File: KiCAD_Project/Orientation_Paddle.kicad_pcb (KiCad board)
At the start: 2 copper layers, 158.7 x 47 mm, 72 parts, among them J1 1-0001205, J2 1-0001156, J3 1-0001156, J4 NP_Conn_01x02_Relief, J5 NP_Conn_01x02_Relief, J6 NP_Conn_01x04, J7 NP_Conn_01x02, J8 1-0000050, J9 1-0000190, Q1 1-0001670, U1 1-0001471, U2 1-0000207, U3 1-0000785, U4 1-0000446, Y1 1-0000721

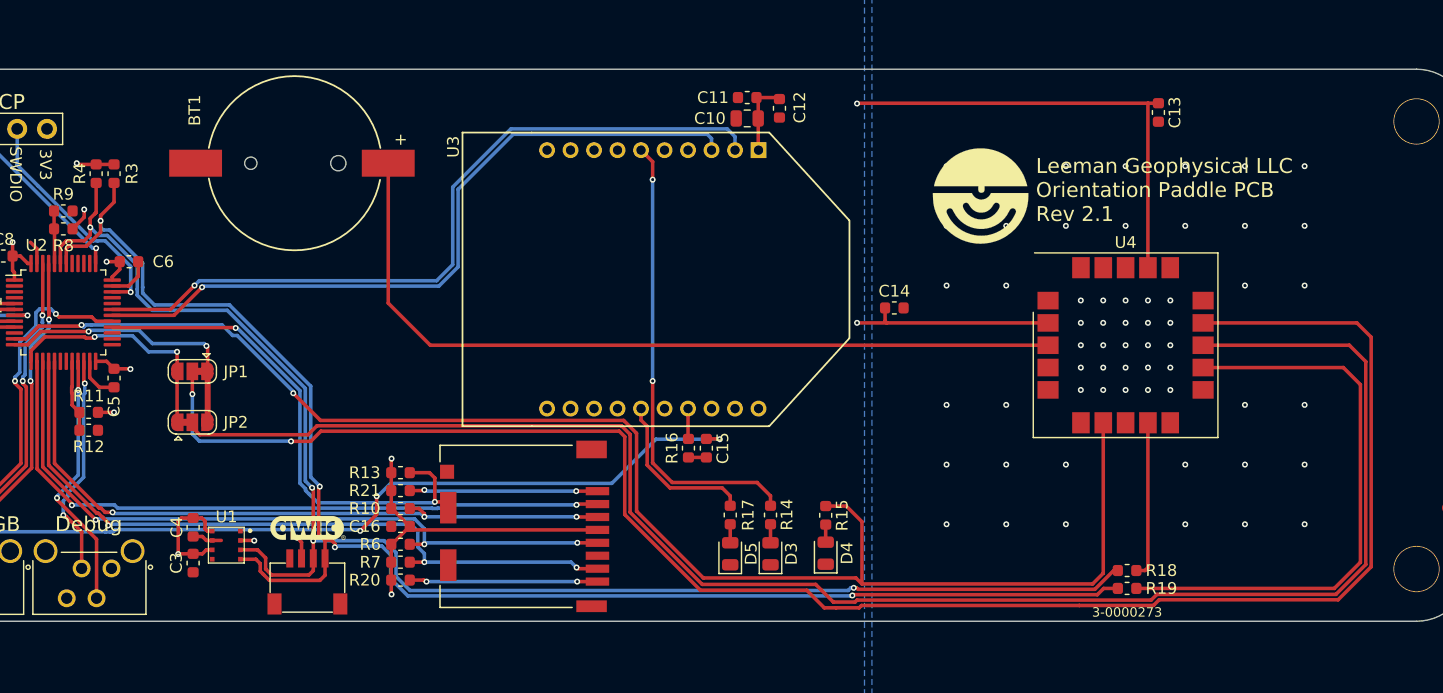
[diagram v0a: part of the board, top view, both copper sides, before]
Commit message: Rev 2.2 Changes: - Issue #2 (Swapped to Push Push SD Holder) - Updated PCB and Revision Numbers - Fixed all DRC/ERC Issues
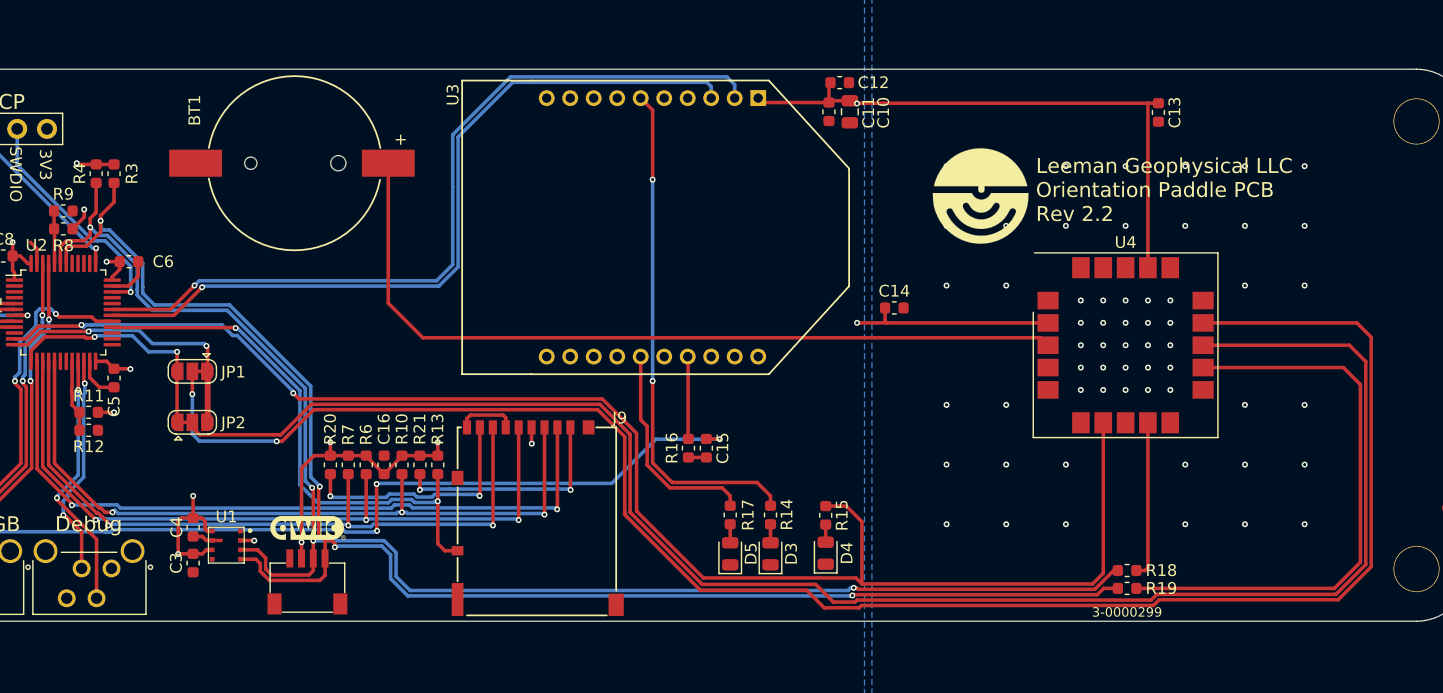
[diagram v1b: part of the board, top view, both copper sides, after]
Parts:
- J9: value 1-0000190 -> 1-0000127; footprint connectors:1-0000190 -> connectors:1-0000127
- JP1, JP2: value SolderJumper_3_Bridged12 -> SolderJumper_3_Open; footprint np_connectors:SolderJumper-3_P1.3mm_Bridged12_RoundedPad1.0x1.5mm -> Jumper:SolderJumper-3_P1.3mm_Open_RoundedPad1.0x1.5mm
- moved R20 11.5 mm to (125.3, 114.3), turned to -90 degrees
- moved J9 9.85 mm to (137.0, 111.1), turned to 0 degrees
- moved R7 9.40 mm to (126.9, 114.3), turned to -90 degrees
- moved C10 8.76 mm to (169.6, 84.3), turned to -90 degrees
- moved R6 7.36 mm to (128.4, 114.3), turned to -90 degrees
- moved C11 7.06 mm to (167.8, 84.3), turned to -90 degrees
- moved C12 5.57 mm to (168.7, 81.8), turned to 0 degrees
- moved C16 5.42 mm to (129.9, 114.3), turned to -90 degrees
- moved J8 4.43 mm to (152.8, 94.1)
- moved U3 4.43 mm to (161.8, 94.1)
- moved R10 3.71 mm to (131.4, 114.3), turned to -90 degrees
- moved R13 3.24 mm to (134.5, 114.3), turned to -90 degrees
- moved R21 2.74 mm to (133.0, 114.3), turned to -90 degrees
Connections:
- J9 pad 9: SD_CD -> GND
- JP1 pad 2: Net-(JP1-C) -> GPS_RX
- JP2 pad 2: Net-(JP2-C) -> GPS_TX
- U4 pad 13: Net-(JP2-C) -> GPS_TX
- U4 pad 14: Net-(JP1-C) -> GPS_RX
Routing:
- net GPS_RX: track 23.9 -> 179.0 mm, vias 2 -> 4
- net Net-(JP1-C): track 152.2 -> 0.00 mm, vias 2 -> 0
- net GPS_TX: track 20.5 -> 167.4 mm
- net Net-(JP2-C): track 144.0 -> 0.00 mm
- net GND: track 21.1 -> 26.2 mm
- net Net-(J9-DAT1): track 16.0 -> 20.8 mm
- net SPI_MOSI: track 58.5 -> 63.1 mm
- net Net-(U3-AD3/DIO3/nSSEL): track 2.60 -> 7.04 mm
- net Net-(U3-Assoc/DIO5): track 14.0 -> 18.5 mm
- net Net-(U3-~{DIO10/PWM0}): track 39.1 -> 43.5 mm
- net XBee_RX: track 64.7 -> 69.1 mm
- net XBee_TX: track 62.4 -> 66.8 mm
- net SD_CS: track 58.5 -> 62.2 mm
- net Net-(J9-DAT2): track 16.0 -> 19.6 mm
- net SD_CD: track 44.0 -> 46.7 mm
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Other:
- board text added: "3-0000299"
- board text added: "Leeman Geophysical LLC Orientation Paddle PCB Rev 2.2"
- board text removed: "3-0000273"
- board text removed: "Leeman Geophysical LLC Orientation Paddle PCB Rev 2.1"

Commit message: Make Rev 2.2 Production Files
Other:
- board text added: "ICP"
- board text removed: "ISCP"
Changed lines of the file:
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@@
 	(title_block
 		(title "Orientation Paddle - NSSL EFM")
-		(date "2025-07-03")
-		(rev "2.1")
+		(date "2026-02-13")
+		(rev "2.2")
 		(company "Leeman Geophysical LLC")
 		(comment 1 "(479) 373-3736")
@@
 			)
 		)
-		(property "Description" "10 (8 + 2) Position Card Connector Secure Digital - microSD™ Surface Mount, Right Angle Gold"
+		(property "Description" ""
 			(at 0 0 0)
 			(layer "F.Fab")
@@
 		)
 	)
-	(gr_text "ISCP"
+	(gr_text "ICP"
 		(at 97.409 83.439 0)
 		(layer "F.SilkS")
@@
 		)
 	)
-	(gr_text "ISCP"
+	(gr_text "ICP"
 		(at 97.409 83.439 0)
 		(layer "B.SilkS")
